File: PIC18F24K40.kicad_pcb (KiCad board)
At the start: 2 copper layers, 22 x 34.5 mm, 21 parts, among them J1 Conn_01x13, J2 Conn_01x13, J3 ICSP, J4 USB_B_Micro, Q1 Q_Photo_NPN, SW1 SW_SPST, U1 FT231XQ, U2 PIC18F24K40-I_ML

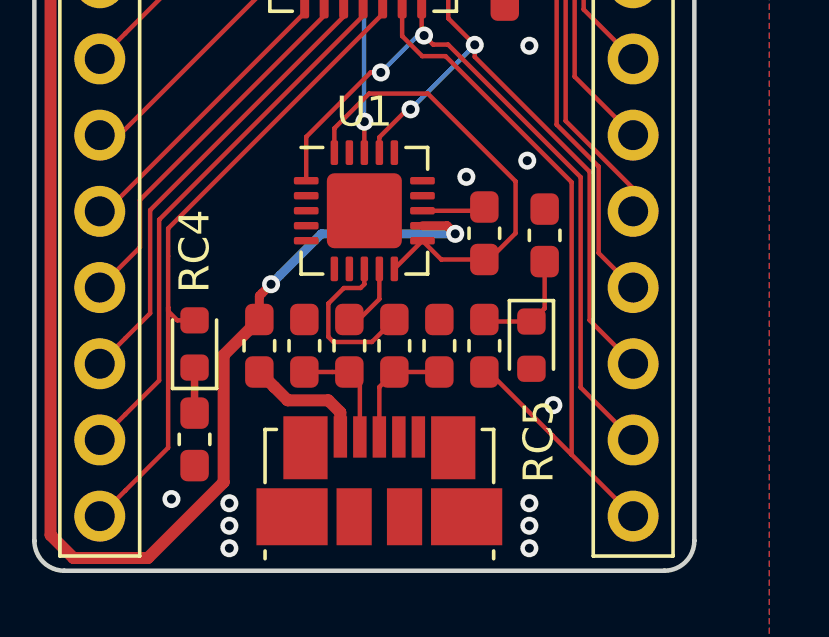
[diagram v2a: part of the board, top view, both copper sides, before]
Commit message: RC5 now connected to the right place
OMG I screwed up the light sensor connection! The boards come in soon...

Schematic and board updated. Will kynar the prototypes
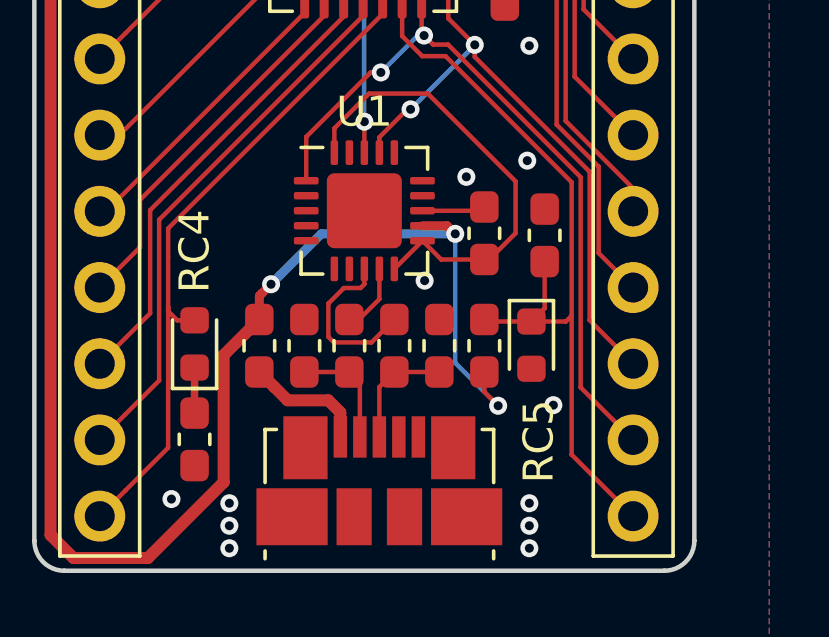
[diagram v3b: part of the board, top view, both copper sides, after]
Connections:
- C6 pad 1: Net-(C6-Pad1) -> /RC5
- Q1 pad 1: Net-(C6-Pad1) -> /RC5
- R5 pad 1: Net-(C6-Pad1) -> /RC5
- R5 pad 2: /RC5 -> VCC
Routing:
- net VCC: track 96.8 -> 104.6 mm, vias 4 -> 5
- net Net-(C6-Pad1): track 3.78 -> 0.00 mm
- net /RC5: track 24.8 -> 25.9 mm
- net GND: vias 13 -> 14
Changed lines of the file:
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@@
     (thickness 1.6)
     (drawings 11)
-    (tracks 256)
+    (tracks 263)
     (zones 0)
     (modules 21)
-    (nets 48)
+    (nets 47)
   )
   (page A4)
@@
   (net 45 "Net-(FB1-Pad2)")
   (net 46 "Net-(D1-Pad1)")
-  (net 47 "Net-(C6-Pad1)")
   (net_class Default "This is the default net class."
     (clearance 0.15)
@@
     (add_net "Net-(C4-Pad1)")
     (add_net "Net-(C5-Pad2)")
-    (add_net "Net-(C6-Pad1)")
     (add_net "Net-(D1-Pad1)")
     (add_net "Net-(FB1-Pad2)")
@@
     )
     (pad 1 smd roundrect (at -0.875 0 90) (size 1.05 0.95) (layers F.Cu F.Paste F.Mask) (roundrect_rratio 0.25)
-      (net 47 "Net-(C6-Pad1)"))
+      (net 14 /RC5))
     (pad 2 smd roundrect (at 0.875 0 90) (size 1.05 0.95) (layers F.Cu F.Paste F.Mask) (roundrect_rratio 0.25)
       (net 2 GND))
@@
     )
     (pad 1 smd roundrect (at -0.7875 0 270) (size 0.875 0.95) (layers F.Cu F.Paste F.Mask) (roundrect_rratio 0.25)
-      (net 47 "Net-(C6-Pad1)"))
+      (net 14 /RC5))
     (pad 2 smd roundrect (at 0.7875 0 270) (size 0.875 0.95) (layers F.Cu F.Paste F.Mask) (roundrect_rratio 0.25)
       (net 2 GND))
@@
     )
     (pad 1 smd roundrect (at -0.875 0 270) (size 1.05 0.95) (layers F.Cu F.Paste F.Mask) (roundrect_rratio 0.25)
-      (net 47 "Net-(C6-Pad1)"))
+      (net 14 /RC5))
     (pad 2 smd roundrect (at 0.875 0 270) (size 1.05 0.95) (layers F.Cu F.Paste F.Mask) (roundrect_rratio 0.25)
-      (net 14 /RC5))
+      (net 1 VCC))
     (model ${KIPRJMOD}/libs/packages3d/R_0603_1608Metric.step
       (at (xyz 0 0 0))
@@
   (segment (start 107.529999 105.830001) (end 106.68 106.68) (width 0.15) (layer F.Cu) (net 13))
   (segment (start 108.96 104.4) (end 107.529999 105.830001) (width 0.15) (layer F.Cu) (net 13))
-  (segment (start 122.41 95.55) (end 122.41 104.63) (width 0.15) (layer F.Cu) (net 14))
+  (segment (start 109.94 100.235) (end 109.92 100.255) (width 0.15) (layer F.Cu) (net 13))
+  (segment (start 108.96 99.8475) (end 108.96 99.72) (width 0.15) (layer F.Cu) (net 13))
+  (segment (start 109.84 100.1525) (end 109.265 100.1525) (width 0.15) (layer F.Cu) (net 13))
+  (segment (start 109.265 100.1525) (end 108.96 99.8475) (width 0.15) (layer F.Cu) (net 13))
+  (segment (start 108.96 99.72) (end 108.96 104.4) (width 0.15) (layer F.Cu) (net 13))
+  (segment (start 108.96 98.0125) (end 108.96 99.72) (width 0.15) (layer F.Cu) (net 13))
+  (segment (start 116.11 89.5775) (end 116.11 89.94) (width 0.15) (layer F.Cu) (net 13))
+  (segment (start 108.96 97.09) (end 108.96 98.0125) (width 0.15) (layer F.Cu) (net 13))
+  (segment (start 116.11 89.94) (end 108.96 97.09) (width 0.15) (layer F.Cu) (net 13))
   (segment (start 117.43 91.347004) (end 118.207004 91.347004) (width 0.15) (layer F.Cu) (net 14))
   (segment (start 122.41 104.63) (end 124.46 106.68) (width 0.15) (layer F.Cu) (net 14))
@@
   (segment (start 116.76 89.5775) (end 116.76 90.677004) (width 0.15) (layer F.Cu) (net 14))
   (segment (start 116.76 90.677004) (end 117.43 91.347004) (width 0.15) (layer F.Cu) (net 14))
-  (segment (start 121.77 103.99) (end 122.41 104.63) (width 0.15) (layer F.Cu) (net 14))
-  (segment (start 119.5 101.875) (end 119.655 101.875) (width 0.15) (layer F.Cu) (net 14))
-  (segment (start 119.655 101.875) (end 121.77 103.99) (width 0.15) (layer F.Cu) (net 14))
+  (segment (start 119.5 101.875) (end 119.655 101.875) (width 0.15) (layer F.Cu) (net 1))
+  (via (at 119.96 103) (size 0.6) (drill 0.3) (layers F.Cu B.Cu) (net 1))
+  (segment (start 119.5 101.875) (end 119.5 102.54) (width 0.15) (layer F.Cu) (net 1))
+  (segment (start 119.5 102.54) (end 119.96 103) (width 0.15) (layer F.Cu) (net 1))
+  (segment (start 118.53 101.57) (end 118.53 97.27) (width 0.15) (layer B.Cu) (net 1))
+  (segment (start 119.96 103) (end 118.53 101.57) (width 0.15) (layer B.Cu) (net 1))
+  (via (at 117.51 98.83) (size 0.6) (drill 0.3) (layers F.Cu B.Cu) (net 2))
   (via (at 116.05 91.89) (size 0.6) (drill 0.3) (layers F.Cu B.Cu) (net 15))
   (segment (start 115.71 91.89) (end 116.05 91.89) (width 0.15) (layer F.Cu) (net 15))
@@
   (segment (start 115 100.125) (end 115.32091 100.125) (width 0.15) (layer F.Cu) (net 41))
   (segment (start 115.32091 100.125) (end 116 99.44591) (width 0.15) (layer F.Cu) (net 41))
-  (segment (start 115.5 98.95) (end 115.5 98.4375) (width 0.15) (layer F.Cu) (net 42))
-  (segment (start 115.37499 99.07501) (end 115.5 98.95) (width 0.15) (layer F.Cu) (net 42))
-  (segment (start 114.818408 99.07501) (end 115.37499 99.07501) (width 0.15) (layer F.Cu) (net 42))
-  (segment (start 114.29999 99.593428) (end 114.818408 99.07501) (width 0.15) (layer F.Cu) (net 42))
-  (segment (start 114.29999 100.70406) (end 114.29999 99.593428) (width 0.15) (layer F.Cu) (net 42))
-  (segment (start 114.47094 100.87501) (end 114.29999 100.70406) (width 0.15) (layer F.Cu) (net 42))
-  (segment (start 115.74999 100.87501) (end 114.47094 100.87501) (width 0.15) (layer F.Cu) (net 42))
-  (segment (start 116.5 100.125) (end 115.74999 100.87501) (width 0.15) (layer F.Cu) (net 42))
   (via (at 115.49 82.57) (size 0.6) (drill 0.3) (layers F.Cu B.Cu) (net 43))
   (segment (start 115.9 80.525) (end 115.499072 80.124072) (width 0.15) (layer F.Cu) (net 43))
@@
   (segment (start 114.7 104.04) (end 114.7 103.22) (width 0.4) (layer F.Cu) (net 45))
   (segment (start 114.7 103.22) (end 114.3 102.82) (width 0.4) (layer F.Cu) (net 45))
-  (segment (start 109.94 100.235) (end 109.92 100.255) (width 0.15) (layer F.Cu) (net 13))
-  (segment (start 108.96 99.8475) (end 108.96 99.72) (width 0.15) (layer F.Cu) (net 13))
-  (segment (start 109.84 100.1525) (end 109.265 100.1525) (width 0.15) (layer F.Cu) (net 13))
-  (segment (start 109.265 100.1525) (end 108.96 99.8475) (width 0.15) (layer F.Cu) (net 13))
-  (segment (start 108.96 99.72) (end 108.96 104.4) (width 0.15) (layer F.Cu) (net 13))
-  (segment (start 108.96 98.0125) (end 108.96 99.72) (width 0.15) (layer F.Cu) (net 13))
-  (segment (start 116.11 89.5775) (end 116.11 89.94) (width 0.15) (layer F.Cu) (net 13))
-  (segment (start 108.96 97.09) (end 108.96 98.0125) (width 0.15) (layer F.Cu) (net 13))
-  (segment (start 116.11 89.94) (end 108.96 97.09) (width 0.15) (layer F.Cu) (net 13))
   (segment (start 109.84 103.245) (end 109.84 101.7275) (width 0.25) (layer F.Cu) (net 46))
-  (segment (start 121.51 99.7525) (end 121.07 100.1925) (width 0.15) (layer F.Cu) (net 47))
-  (segment (start 121.51 98.195) (end 121.51 99.7525) (width 0.15) (layer F.Cu) (net 47))
-  (segment (start 119.5675 100.1925) (end 119.5 100.125) (width 0.15) (layer F.Cu) (net 47))
-  (segment (start 121.07 100.1925) (end 119.5675 100.1925) (width 0.15) (layer F.Cu) (net 47))
+  (segment (start 121.51 99.7525) (end 121.07 100.1925) (width 0.15) (layer F.Cu) (net 14))
+  (segment (start 121.51 98.195) (end 121.51 99.7525) (width 0.15) (layer F.Cu) (net 14))
+  (segment (start 119.5675 100.1925) (end 119.5 100.125) (width 0.15) (layer F.Cu) (net 14))
+  (segment (start 121.07 100.1925) (end 119.5675 100.1925) (width 0.15) (layer F.Cu) (net 14))
+  (segment (start 122.41 95.55) (end 122.41 100) (width 0.15) (layer F.Cu) (net 14))
+  (segment (start 122.41 100) (end 122.41 104.63) (width 0.15) (layer F.Cu) (net 14))
+  (segment (start 122.2175 100.1925) (end 122.41 100) (width 0.15) (layer F.Cu) (net 14))
+  (segment (start 121.07 100.1925) (end 122.2175 100.1925) (width 0.15) (layer F.Cu) (net 14))
+  (segment (start 115.5 98.95) (end 115.5 98.4375) (width 0.15) (layer F.Cu) (net 42))
+  (segment (start 115.735 100.89) (end 114.48593 100.89) (width 0.15) (layer F.Cu) (net 42))
+  (segment (start 114.48593 100.89) (end 114.29999 100.70406) (width 0.15) (layer F.Cu) (net 42))
+  (segment (start 115.37499 99.07501) (end 115.5 98.95) (width 0.15) (layer F.Cu) (net 42))
+  (segment (start 116.5 100.125) (end 115.735 100.89) (width 0.15) (layer F.Cu) (net 42))
+  (segment (start 114.29999 99.593428) (end 114.818408 99.07501) (width 0.15) (layer F.Cu) (net 42))
+  (segment (start 114.29999 100.70406) (end 114.29999 99.593428) (width 0.15) (layer F.Cu) (net 42))
+  (segment (start 114.818408 99.07501) (end 115.37499 99.07501) (width 0.15) (layer F.Cu) (net 42))
   (zone (net 2) (net_name GND) (layer B.Cu) (hatch edge 0.508)
     (connect_pads (clearance 0.2))
